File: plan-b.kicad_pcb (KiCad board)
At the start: 4 copper layers, 14 x 42.1 mm, 67 parts, among them J1 HRO_TYPE-C-31-M-14, J2 Battery, J3 rgb, J4 columns, J5 Conn_01x10, J6 rows, J7 sensor, J8 Conn_ARM_SWD_TagConnect_TC203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, J9 Conn_01x05_Pin, SW1 Battery, SW2 Reset, U1 nRF52840_CKAA, U2 nPM1100-CAAx, U3 TPS22916BYFPT, X1 32MHz, X2 32.768kHz

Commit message: Dumping the reference layouts into the PCB
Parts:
- removed the U1 at (151.9, 78.9)
- removed U2: nPM1100-CAAx, nRF Devices$:BGA25C40P5X5_200X200X50
- removed U3: TPS22916BYFPT, TPS22916 load switch:BGA4C40P2X2_77X77X50
- added C1: 12pF, 0402:CAPC1005X04L, F.Cu at (185.2, 98.8)
- added C1: 2.2µF, Capacitors$:CAPC1608X06L, F.Cu at (179.6, 68.1)
- added C10: N.C., Passive:CAPC1005X04L, F.Cu at (185.5, 95.2)
- added C11: 100pF, Passive:CAPC1005X04L, F.Cu at (185.7, 96.6)
- added C12: 100nF, Passive:CAPC1005X04L, F.Cu at (188.5, 97.2)
- added C13: N.C., Passive:CAPC1005X04L, F.Cu at (190.6, 98.8)
- added C14: 1.0µF, Passive:CAPC1608X06L, F.Cu at (197.0, 96.4)
- added C15: 1.0µF, Passive:CAPC1608X06L, F.Cu at (193.6, 98.5)
- added C16: 47nF, Passive:CAPC1005X04L, F.Cu at (193.6, 97.5)
- added C17: 12pF, Passive:CAPC1005X04L, F.Cu at (200.2, 93.7)
- added C18: 12pF, Passive:CAPC1005X04L, F.Cu at (197.6, 92.3)
- added C19: 4.7µF, Passive:CAPC1608X06L, F.Cu at (197.4, 87.7)
- added C2: 10µF, Capacitors$:CAPC1608X06L, F.Cu at (172.7, 66.2)
- added C2: 12pF, 0402:CAPC1005X04L, F.Cu at (188.8, 98.8)
- added C20: 4.7µF, Passive:CAPC1608X06L, F.Cu at (195.0, 87.0)
- added C21: 4.7µF, Passive:CAPC1608X06L, F.Cu at (193.9, 87.0)
- added C3: 0.8pF, Nordic Passive DB:CAPC1005X04L, F.Cu at (186.7, 94.0)
- added C3: 10µF, Passive:CAPC1608X06L, F.Cu at (180.8, 68.7)
- added C4: 0.5pF, Passive:CAPC1005X04L, F.Cu at (183.8, 94.0)
- added C4: 10µF, Capacitors$:CAPC1608X06L, F.Cu at (176.0, 66.7)
- added C5: 1.0µF, CAPC0603X03L_C:CAPC0603X03L_C, F.Cu at (180.5, 70.5)
- added C5: 100nF, 0402:CAPC1005X04L, F.Cu at (197.1, 95.3)
- added C6: 4.7µF, Passive:CAPC1608X06L, F.Cu at (198.7, 87.7)
- added C7: 100nF, 0402:CAPC1005X04L, F.Cu at (191.0, 87.6)
- added C8: 100nF, 0402:CAPC1005X04L, F.Cu at (188.2, 87.6)
- added C9: 820pF, 0402:CAPC1005X04L, F.Cu at (185.3, 90.7)
- added J6: Net tie, 2 pin starpoint:2 PIN STARPOINT, F.Cu at (174.1, 67.5)
- added L1: 2.2µH, Parts$:INDC2016X10N, F.Cu at (175.0, 64.9)
- added L1: 4.7nH, Inductors$:INDC1005X04L, F.Cu at (185.3, 93.4)
- added L2: 10µH, 0603:INDC1608X06L, F.Cu at (195.5, 98.3)
- added L3: 15nH, 0402:INDC1005X04L, F.Cu at (195.0, 100.1)
- added L4: 10µH, Passive:INDC1608X06L, F.Cu at (196.2, 87.7)
- added LD1: L0603R, pcblib:LED_0603_R, F.Cu at (176.7, 74.1)
- added LD2: L0603G, pcblib:LED_0603_G, F.Cu at (175.3, 74.1)
- added LD3: L0603R, pcblib:LED_0603_R, F.Cu at (181.9, 66.6)
- added R3: 1k, Passive:RESC0603X03L_C, F.Cu at (181.7, 68.4)
- added U1: nRF52840-QIAA, AQFN50P700X700X85_HS-74N:AQFN50P700X700X85_HS-74N, F.Cu at (191.2, 92.7)
- added U1: nPM1100-QDAx, Parts$:QFN50P400X400X80_HS-25N, F.Cu at (176.3, 69.9)
- added X1: 32MHz, Crystal_Osc$:BT-XTAL_2016, F.Cu at (187.0, 98.8)
- added X2: 32.768kHz, pcblib:XTAL_3215, F.Cu at (197.8, 93.7)
- C1, C17, C18, C2, C22, C3, C30, C37, C38, C5, C7, C8, C9: footprint Capacitor_SMD:C_0201_0603Metric -> Capacitor_SMD:C_0402_1005Metric
- R11, R14, R15, R16, R21, R22, R3, R32, R33, R39, R8, R_BLE1, R_DIV1, R_DIV2, R_ICHG1: footprint Resistor_SMD:R_0201_0603Metric -> Resistor_SMD:R_0402_1005Metric
- moved R_ICHG1 34.9 mm to (178.9, 73.2), turned to 180 degrees
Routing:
- net VDD: track 72.8 -> 0.00 mm, vias 9 -> 0
- net VDD_NRF: track 0.00 -> 50.6 mm, vias 0 -> 6
- net RST: track 40.5 -> 0.00 mm, vias 4 -> 0
- net VBAT: track 38.5 -> 4.30 mm, vias 2 -> 0
- net GND: track 39.8 -> 12.2 mm, vias 60 -> 47
- net D-: track 26.1 -> 6.46 mm, vias 3 -> 0
- net D+: track 26.0 -> 6.39 mm, vias 3 -> 0
- net DEC4_6: track 0.00 -> 19.2 mm, vias 0 -> 2
- net Net-(J2-Pin_1): track 17.9 -> 0.00 mm, vias 1 -> 0
- net Row 4: track 17.3 -> 0.00 mm, vias 3 -> 0
- net Row 3: track 15.8 -> 0.00 mm, vias 3 -> 0
- net LCD CS: track 15.6 -> 0.00 mm
- net Row 1: track 15.3 -> 0.00 mm, vias 3 -> 0
- net Row 0: track 15.3 -> 0.00 mm, vias 3 -> 0
- net LCD DATA: track 15.2 -> 0.00 mm
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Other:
- board size 14 x 42.1 mm -> 82.4 x 70 mm

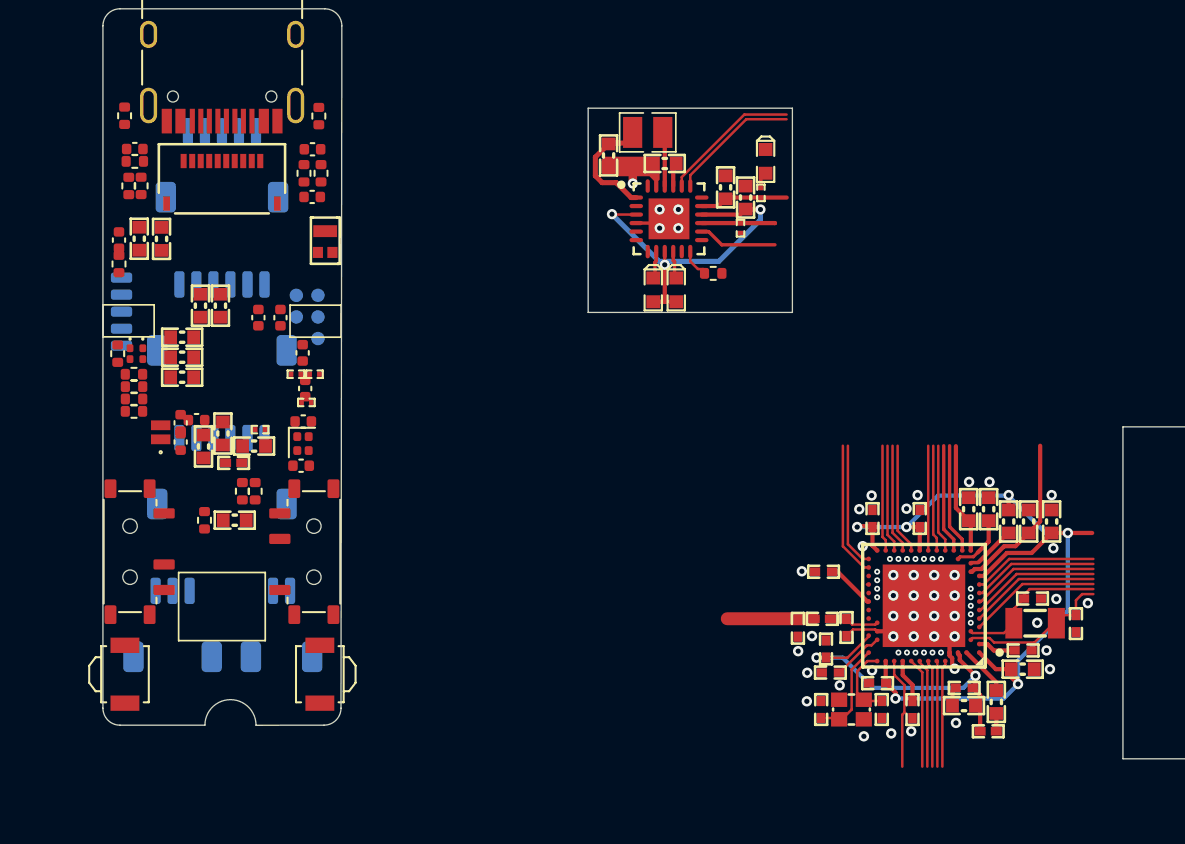
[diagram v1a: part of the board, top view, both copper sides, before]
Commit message: Adding some basic libarary components
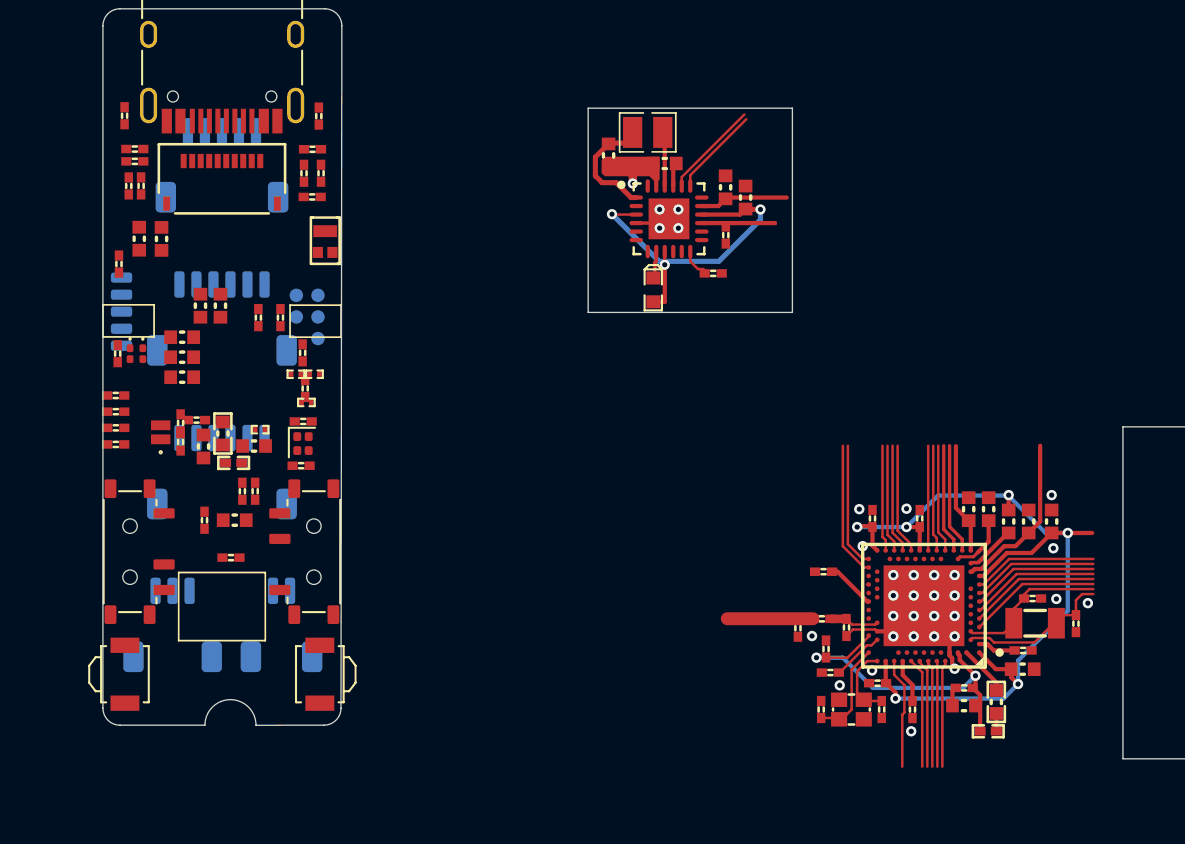
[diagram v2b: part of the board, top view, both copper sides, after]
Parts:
- removed LD1: L0603R, pcblib:LED_0603_R
- removed the LD3 at (181.9, 66.6)
- removed the R3 at (181.7, 68.4)
- C1, C17, C18, C2, C22, C3, C30, C37, C38, C5, C7, C8, C9: footprint Capacitor_SMD:C_0402_1005Metric -> Library:C_0402_1005
- C1, C2, C5, C7, C8, C9: footprint 0402:CAPC1005X04L -> Library:C_0402_1005
- C1, C2, C23, C24, C4: footprint Capacitors$:CAPC1608X06L -> Library:C_0603_1608
- C10, C11, C12, C13, C16, C17, C18, C4: footprint Passive:CAPC1005X04L -> Library:C_0402_1005
- C14 (x2), C15 (x2), C19 (x2), C20 (x2), C21 (x2), C3, C4, C6 (x2): footprint Passive:CAPC1608X06L -> Library:C_0603_1608
- C3: footprint Nordic Passive DB:CAPC1005X04L -> Library:C_0402_1005
- C5: footprint CAPC0603X03L_C:CAPC0603X03L_C -> Library:C_0402_1005
- FB1, FB2, R11, R14, R15, R16, R21, R22, R3, R32, R33, R39, R8, R_BLE1, R_DIV1, R_DIV2, R_ICHG1: footprint Resistor_SMD:R_0402_1005Metric -> Library:R_0402_1005
- L1: footprint Inductors$:INDC1005X04L -> Library:L_0402_1005
- L4 (x2): footprint Passive:INDC1608X06L -> Library:L_0603_1608
- moved C22 19.8 mm to (150.5, 89.8), turned to 0 degrees
- moved R16 2.22 mm to (143.8, 83.2)
- moved R15 2.00 mm to (143.8, 82.2)
- moved R14 1.82 mm to (143.8, 81.3)
- moved R11 1.64 mm to (143.8, 80.3)
- moved C5 0.95 mm to (179.6, 70.9)
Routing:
- net P1.07: track 10.0 -> 0.00 mm, vias 1 -> 0
- net P1.05: track 9.40 -> 0.00 mm, vias 1 -> 0
- net P1.03: track 8.78 -> 0.00 mm, vias 1 -> 0
- net P1.01: track 8.17 -> 0.00 mm, vias 1 -> 0
- net P0.27: track 8.02 -> 0.00 mm, vias 1 -> 0
- net P0.05/AIN3: track 7.94 -> 0.00 mm, vias 1 -> 0
- net P0.07: track 7.86 -> 0.00 mm, vias 1 -> 0
- net P1.08: track 7.77 -> 0.00 mm, vias 1 -> 0
- net P0.11: track 7.71 -> 0.00 mm, vias 1 -> 0
- net P0.25: track 7.61 -> 0.00 mm, vias 1 -> 0
- net P0.23: track 7.52 -> 0.00 mm, vias 1 -> 0
- net P0.21: track 7.44 -> 0.00 mm, vias 1 -> 0
- net P0.19: track 7.36 -> 0.00 mm, vias 1 -> 0
- net P0.18/RESET: track 7.28 -> 0.00 mm, vias 1 -> 0
- net P1.11: track 7.23 -> 0.00 mm, vias 1 -> 0
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
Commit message: Cleaning up more components
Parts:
- removed the C1 at (154.8, 81.8)
- removed C10, C13: N.C., Library:C_0402_1005
- removed the C12 at (155.0, 80.7)
- removed the C14 at (148.9, 83.3)
- removed the C15 at (151.9, 83.3)
- removed the C16 at (152.2, 82.3)
- removed the C17 at (147.6, 83.1)
- removed the C18 at (147.6, 81.9)
- removed the C19 at (147.7, 76.9)
- removed the C2 at (154.7, 84.5)
- removed the C20 at (149.9, 75.0)
- removed the C21 at (148.7, 75.0)
- removed the C23 at (145.1, 71.1)
- removed the C24 at (146.4, 71.1)
- removed the C3 at (154.9, 79.9)
- removed the C5 at (148.5, 81.8)
- removed the C6 at (147.7, 79.2)
- removed the C7 at (152.1, 75.8)
- removed the C8 at (153.4, 75.8)
- removed the C9 at (154.7, 77.8)
- removed the L1 at (154.3, 79.1)
- removed the L2 at (150.1, 82.6)
- removed the L3 at (150.7, 84.3)
- removed the L4 at (147.7, 78.1)
- removed the L5 at (155.4, 79.1)
- removed R_BLE1: 470k, Library:R_0402_1005
- L2: footprint 0603:INDC1608X06L -> Library:L_0603_1608
- L3: footprint 0402:INDC1005X04L -> Library:L_0402_1005
- moved R3 56.2 mm to (200.1, 70.8), turned to 180 degrees
- moved LD2 26.6 mm to (201.9, 76.6), turned to 0 degrees
- moved X2 26.4 mm to (171.0, 92.1)
- moved C26 24.9 mm to (194.0, 79.2), turned to 180 degrees
- moved J6 23.5 mm to (195.2, 77.8), turned to 180 degrees
- moved U1 22.2 mm to (197.7, 75.7), turned to 90 degrees
- moved R_ICHG 22.0 mm to (200.9, 73.1), turned to -90 degrees
- moved X1 22.0 mm to (172.5, 96.1)
- moved L5 21.3 mm to (192.6, 76.9), turned to 90 degrees
- moved C25 20.6 mm to (194.4, 75.9), turned to 90 degrees
- moved AE1 20.4 mm to (135.8, 71.1)
- moved C22 19.1 mm to (198.6, 72.3), turned to 180 degrees
- moved C24 16.8 mm to (195.8, 72.3), turned to 0 degrees
- moved C23 15.9 mm to (196.4, 71.2), turned to 0 degrees
- moved J9 15.7 mm to (161.5, 75.5)
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- renumbered C5 to C22, C3 to C23, C1 to C24, C4 to C25, C2 to C26, L1 to L5, R_ICHG1 to R_ICHG
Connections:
- R3 pad 1: Net-(U2-NTC) -> (no net)
- R3 pad 2: GND -> (no net)
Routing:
- net DEC4_6: track 19.2 -> 16.3 mm
- net NetC13_1: track 2.59 -> 0.00 mm
- net P0.00/XL1: track 9.04 -> 7.00 mm
- net NetC9_1: track 2.87 -> 1.64 mm
- net GND: vias 33 -> 31
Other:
- board text added: "${REFERENCE}"

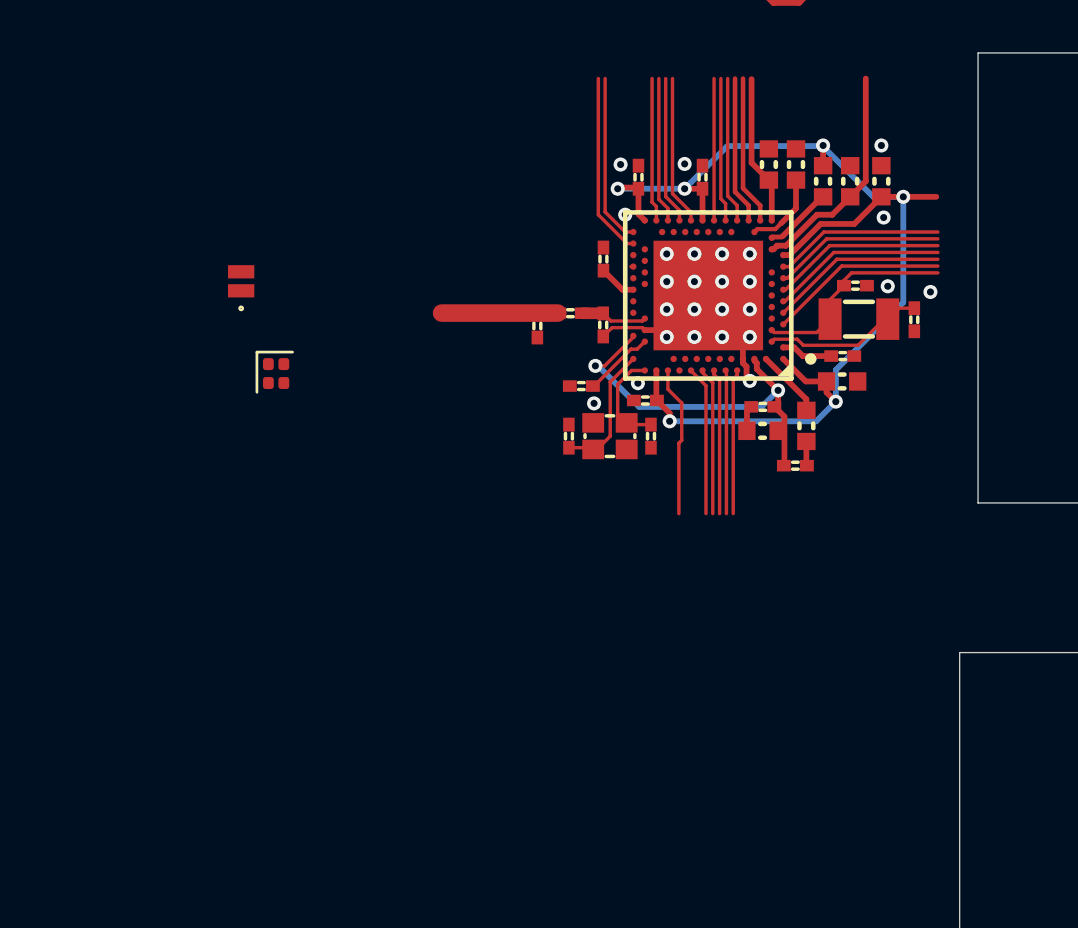
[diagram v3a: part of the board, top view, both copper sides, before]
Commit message: Relinking the schematics and the PCB again
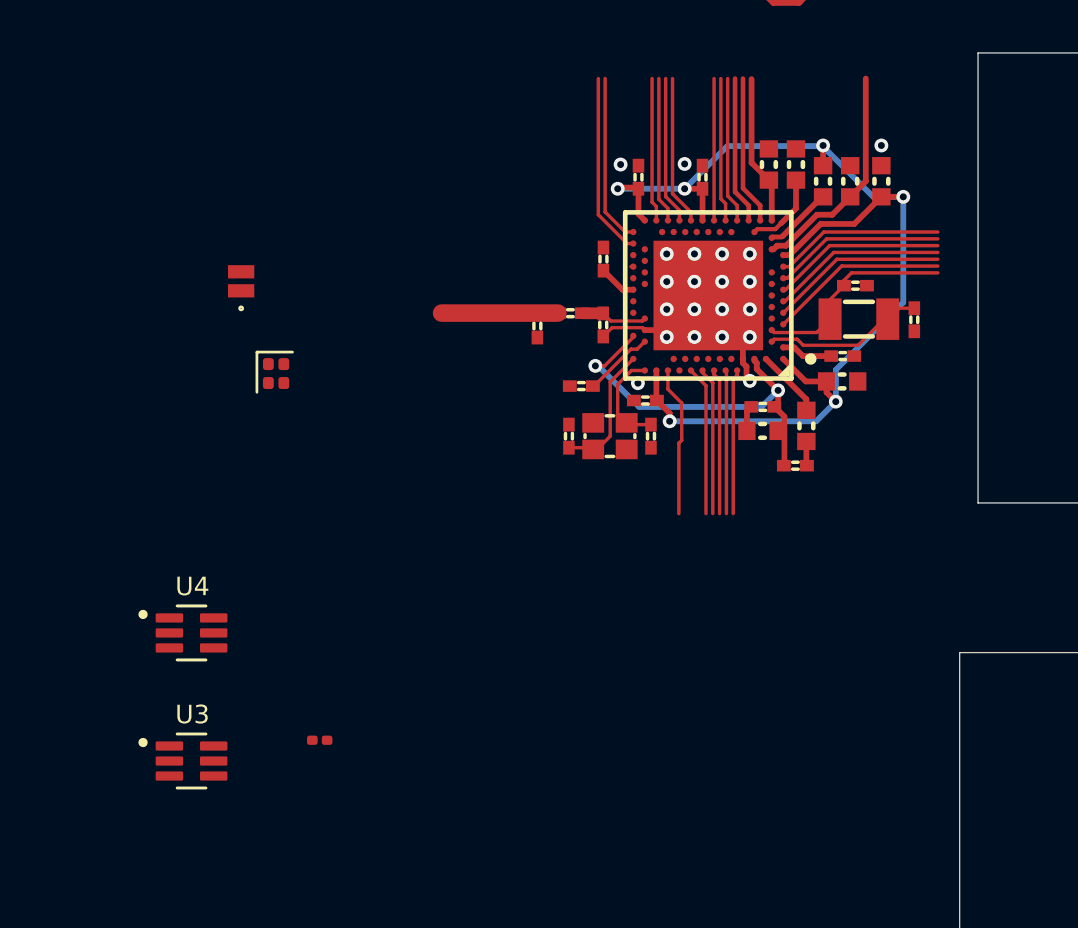
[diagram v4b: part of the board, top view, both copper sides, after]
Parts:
- added R_BLE1: 470k, Resistor_SMD:R_0201_0603Metric, F.Cu at (174.4, 112.0)
- added U3: TPS22919DCKR, TPS22919:SOT65P210X110-6N, F.Cu at (168.8, 112.8)
- added U4: TPS22919DCKR, TPS22919:SOT65P210X110-6N, F.Cu at (168.8, 107.3)
- C3: value 0.8pF -> 0.8 pF
- C4: value 0.5pF -> 0.5 pF
- J99: renamed from J6; value Net tie -> rows
- L1: value 4.7nH -> 4.7 nH
- LD2: value L0603G -> L0603G (Amber)
- R_DIV1: value 2M -> 1.5M
- R_DIV2: value 806k -> 220k
- U1: value nPM1100-QDAx -> nRF52840-QIAA
- renumbered C4 to C44
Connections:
- net DEC1 renamed Net-(U1-DEC1)
- net DEC3 renamed Net-(U1-DEC3)
- net DEC4_6 renamed Net-(U1-DEC4)
- net LCD CLK renamed CLK
- net LCD CS renamed CS
- net LCD DATA renamed DATA
- net NetC20_1 renamed Net-(U1-DECUSB)
- net NetC3_2 renamed Net-(U1-ANT)
- net NetC9_1 renamed Net-(U1-DEC5)
- net NetL2_1 renamed Net-(L2-Pad1)
- net NetL2_2 renamed Net-(U1-DCC)
- net NetL4_2 renamed Net-(U1-DCCH)
- C1 pad 1: XC1 -> Net-(U1-XC1)
- C12 pad 1: VDD_NRF -> VDD
- C14 pad 1: VDD_NRF -> VDD
- C17 pad 1: P0.00/XL1 -> Net-(U1-P0.00/XL1)
- C18 pad 1: P0.01/XL2 -> Net-(U1-P0.01/XL2)
- C19 pad 1: VDD_HV -> VSYS
- C2 pad 1: XC2 -> Net-(U1-XC2)
- C25 pad 2: NetC4_2 -> Net-(U2-DEC)
- C26 pad 2: VOUT -> 1.8v
- C4 pad 2: RF -> /MCU/RF
- C6 pad 1: VDD_NRF -> VDD
- C7 pad 1: VDD_NRF -> VDD
- C8 pad 1: VDD_NRF -> VDD
- J7 pad 1: VDD -> /Optical Sensor/VDD
- J99 pad 1: GND -> Row 0
- J99 pad 2: PVSS -> Row 1
- L1 pad 2: RF -> /MCU/RF
- L4 pad 1: VDD_NRF -> VDD
- L5 pad 1: VOUT -> 1.8v
- L5 pad 2: NetL1_2 -> Net-(U2-SW)
- LD2 pad 1: CHG -> Net-(LD2-C)
- LD2 pad 1: /PSU/CHG -> Net-(LD2-C)
- R3 pad 1: (no net) -> Net-(U2-NTC)
- R3 pad 2: (no net) -> GND
- R_DIV1 pad 1: VBAT -> Net-(U3-QOD)
- U1 pad A10: P0.29/AIN5 -> unconnected-(U1-P0.29/AIN5-PadA10)
- U1 pad A12: P0.02/AIN0 -> unconnected-(U1-P0.02/AIN0-PadA12)
- U1 pad A14: P1.15 -> unconnected-(U1-P1.15-PadA14)
- U1 pad A16: P1.13 -> unconnected-(U1-P1.13-PadA16)
- U1 pad A18: NetC13_1 -> unconnected-(U1-DEC2-PadA18)
- U1 pad A20: P1.10 -> unconnected-(U1-P1.10-PadA20)
- U1 pad A22: VDD_NRF -> VDD
- U1 pad A23: XC2 -> Net-(U1-XC2)
- U1 pad A8: P0.31/AIN7 -> unconnected-(U1-P0.31/AIN7-PadA8)
- U1 pad AA24: SWDCLK -> SWCLK
- U1 pad AC11: P0.16 -> unconnected-(U1-P0.16-PadAC11)
- U1 pad AC13: P0.18/RESET -> RST
- U1 pad AC15: P0.19 -> unconnected-(U1-P0.19-PadAC15)
- U1 pad AC17: P0.21 -> unconnected-(U1-P0.21-PadAC17)
- U1 pad AC19: P0.23 -> unconnected-(U1-P0.23-PadAC19)
- U1 pad AC21: P0.25 -> unconnected-(U1-P0.25-PadAC21)
- U1 pad AC9: P0.14 -> unconnected-(U1-P0.14-PadAC9)
- U1 pad AD10: P0.15 -> unconnected-(U1-P0.15-PadAD10)
- U1 pad AD12: P0.17 -> unconnected-(U1-P0.17-PadAD12)
- U1 pad AD14: VDD_NRF -> VDD
- U1 pad AD16: P0.20 -> unconnected-(U1-P0.20-PadAD16)
- U1 pad AD18: P0.22 -> unconnected-(U1-P0.22-PadAD18)
- U1 pad AD20: P0.24 -> unconnected-(U1-P0.24-PadAD20)
- U1 pad AD22: P1.00 -> unconnected-(U1-P1.00-PadAD22)
- U1 pad AD23: VDD_NRF -> VDD
- U1 pad AD8: P0.13 -> unconnected-(U1-P0.13-PadAD8)
- U1 pad B1: VDD_NRF -> VDD
- U1 pad B11: P0.28/AIN4 -> unconnected-(U1-P0.28/AIN4-PadB11)
- U1 pad B13: P0.03/AIN1 -> unconnected-(U1-P0.03/AIN1-PadB13)
- U1 pad B15: P1.14 -> unconnected-(U1-P1.14-PadB15)
- U1 pad B17: P1.12 -> unconnected-(U1-P1.12-PadB17)
- U1 pad B19: P1.11 -> unconnected-(U1-P1.11-PadB19)
- U1 pad B24: XC1 -> Net-(U1-XC1)
- U1 pad B9: P0.30/AIN6 -> unconnected-(U1-P0.30/AIN6-PadB9)
- U1 pad D2: P0.00/XL1 -> Net-(U1-P0.00/XL1)
- U1 pad F2: P0.01/XL2 -> Net-(U1-P0.01/XL2)
- U1 pad G1: P0.26 -> unconnected-(U1-P0.26-PadG1)
- U1 pad H2: P0.27 -> unconnected-(U1-P0.27-PadH2)
- U1 pad J1: P0.04/AIN2 -> unconnected-(U1-P0.04/AIN2-PadJ1)
- U1 pad J24: P0.10/NFC2 -> unconnected-(U1-P0.10/NFC2-PadJ24)
- U1 pad K2: P0.05/AIN3 -> unconnected-(U1-P0.05/AIN3-PadK2)
- U1 pad L1: P0.06 -> unconnected-(U1-P0.06-PadL1)
- U1 pad L24: P0.09/NFC1 -> unconnected-(U1-P0.09/NFC1-PadL24)
- U1 pad M2: P0.07 -> unconnected-(U1-P0.07-PadM2)
- U1 pad N1: P0.08 -> unconnected-(U1-P0.08-PadN1)
- U1 pad P2: P1.08 -> unconnected-(U1-P1.08-PadP2)
- U1 pad P23: P1.07 -> unconnected-(U1-P1.07-PadP23)
- U1 pad R1: P1.09 -> unconnected-(U1-P1.09-PadR1)
- U1 pad R24: P1.06 -> unconnected-(U1-P1.06-PadR24)
- U1 pad T2: P0.11 -> unconnected-(U1-P0.11-PadT2)
- U1 pad T23: P1.05 -> unconnected-(U1-P1.05-PadT23)
- U1 pad U1: P0.12 -> unconnected-(U1-P0.12-PadU1)
- U1 pad U24: P1.04 -> unconnected-(U1-P1.04-PadU24)
- U1 pad V23: P1.03 -> unconnected-(U1-P1.03-PadV23)
- U1 pad W1: VDD_NRF -> VDD
- U1 pad W24: P1.02 -> unconnected-(U1-P1.02-PadW24)
- U1 pad Y2: VDD_HV -> VSYS
- U1 pad Y23: P1.01 -> unconnected-(U1-P1.01-PadY23)
- U1 pad 1: VOUT -> (no net)
- U1 pad 10: ERR -> (no net)
- U1 pad 11: SHPHLD -> (no net)
- U1 pad 12: NetR_ICHG_2 -> (no net)
- U1 pad 14: NetJ1_2 -> (no net)
- U1 pad 15: VBAT -> (no net)
- U1 pad 16: VSYS -> (no net)
- U1 pad 17: VBUS -> (no net)
- U1 pad 19: D_N -> (no net)
- U1 pad 2: GND -> (no net)
- U1 pad 20: D_P -> (no net)
- U1 pad 21: NetC4_2 -> (no net)
- U1 pad 22: NetL1_2 -> (no net)
- U1 pad 23: PVSS -> (no net)
- U1 pad 25: GND -> (no net)
- U1 pad 3: VSYS -> (no net)
- U1 pad 4: GND -> (no net)
- U1 pad 5: ISET -> (no net)
- U1 pad 6: SHPACT -> (no net)
- U1 pad 7: MODE -> (no net)
- U1 pad 8: CHG -> (no net)
- U1 pad 9: VSYS -> (no net)
- X1 pad 1: XC1 -> Net-(U1-XC1)
- X1 pad 2: GND -> unconnected-(X1-GND-Pad2)
- X1 pad 3: XC2 -> Net-(U1-XC2)
- X1 pad 4: GND -> unconnected-(X1-GND-Pad4)
- X2 pad 1: P0.00/XL1 -> Net-(U1-P0.00/XL1)
- X2 pad 2: P0.01/XL2 -> Net-(U1-P0.01/XL2)
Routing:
- net VDD_NRF: track 50.6 -> 0.00 mm, vias 6 -> 0
- net VDD: track 0.00 -> 49.1 mm, vias 0 -> 6
- net (no net): track 0.00 -> 11.0 mm
- net VDD_HV: track 9.75 -> 0.00 mm
- net VSYS: track 20.0 -> 29.8 mm
- net P0.01/XL2: track 8.94 -> 0.00 mm
- net Net-(U1-P0.01/XL2): track 0.00 -> 8.94 mm
- net SWDCLK: track 7.93 -> 0.00 mm
- net SWCLK: track 0.00 -> 7.93 mm
- net unconnected-(U1-P0.26-PadG1): track 0.00 -> 7.75 mm
- net P0.26: track 7.75 -> 0.00 mm
- net unconnected-(U1-P0.04/AIN2-PadJ1): track 0.00 -> 7.66 mm
- net P0.04/AIN2: track 7.66 -> 0.00 mm
- net unconnected-(U1-P0.06-PadL1): track 0.00 -> 7.58 mm
- net P0.06: track 7.58 -> 0.00 mm
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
